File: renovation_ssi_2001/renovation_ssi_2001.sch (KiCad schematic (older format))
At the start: 70 parts, among them J1 KLPX-0848A-2-B, J2 DB15_Female, J4 Bus_ISA_8bit, J5 Pins_02x04, J6 Pins_02x03, J7 SID_Socket, Q1 PN2222A, Q2 PN2222A, U1 74LS74, U10 74LS138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

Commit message: corrections and improvements
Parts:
- added C21: 100nF, Capacitor_SMD:C_0603_1608Metric, symbol Device:C
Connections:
- net +12V: now also C21.1
- net GND: now also C21.2
- net LOWPASS: now also U12.40 (PB4); no longer U12.39 (PB3)
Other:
- moved on the sheet: C17, C18, C19, JP2, R10, R9, U11
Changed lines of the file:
@@
 Sheet 1 1
 Title "RENOVATION SSI-2001"
-Date "2020-02-16"
+Date "2020-03-08"
 Rev ""
 Comp "Benedikt Freisen"
@@
 Wire Wire Line
 	12000 4500 12400 4500
-Text Label 12650 7500 2    50   ~ 0
+Text Label 12650 7600 2    50   ~ 0
 LOWPASS
 Text Label 12400 4800 3    50   ~ 0
@@
 NoConn ~ 12650 7300
 NoConn ~ 12650 7400
-NoConn ~ 12650 7600
+NoConn ~ 12650 7500
 NoConn ~ 12650 7800
 NoConn ~ 12650 7900
@@
 L Device:R R9
 U 1 1 5E182A07
-P 12000 2550
-F 0 "R9" H 12070 2596 50  0000 L CNN
-F 1 "10k" H 12070 2505 50  0000 L CNN
-F 2 "Resistor_SMD:R_0603_1608Metric" V 11930 2550 50  0001 C CNN
-F 3 "~" H 12000 2550 50  0001 C CNN
-	1    12000 2550
+P 12500 2550
+F 0 "R9" H 12570 2596 50  0000 L CNN
+F 1 "10k" H 12570 2505 50  0000 L CNN
+F 2 "Resistor_SMD:R_0603_1608Metric" V 12430 2550 50  0001 C CNN
+F 3 "~" H 12500 2550 50  0001 C CNN
+	1    12500 2550
 	1    0    0    -1
 $EndComp
@@
 L Device:R R10
 U 1 1 5E183562
-P 12000 2850
-F 0 "R10" H 12070 2896 50  0000 L CNN
-F 1 "1k" H 12070 2805 50  0000 L CNN
-F 2 "Resistor_SMD:R_0603_1608Metric" V 11930 2850 50  0001 C CNN
-F 3 "~" H 12000 2850 50  0001 C CNN
-	1    12000 2850
+P 12500 2850
+F 0 "R10" H 12570 2896 50  0000 L CNN
+F 1 "1k" H 12570 2805 50  0000 L CNN
+F 2 "Resistor_SMD:R_0603_1608Metric" V 12430 2850 50  0001 C CNN
+F 3 "~" H 12500 2850 50  0001 C CNN
+	1    12500 2850
 	1    0    0    -1
 $EndComp
@@
 L Jumper:SolderJumper_2_Open JP2
 U 1 1 5E43CCF4
-P 14800 2400
-F 0 "JP2" H 14800 2605 50  0000 C CNN
-F 1 "SolderJumper_2_Open" H 14800 2514 50  0000 C CNN
-F 2 "Jumper:SolderJumper-2_P1.3mm_Open_RoundedPad1.0x1.5mm" H 14800 2400 50  0001 C CNN
-F 3 "~" H 14800 2400 50  0001 C CNN
-	1    14800 2400
-	1    0    0    -1
-$EndComp
-Wire Wire Line
-	12000 2400 11800 2400
-Wire Wire Line
-	11500 2700 12000 2700
-Connection ~ 12000 2700
-Connection ~ 12000 2400
-Wire Wire Line
-	12500 2400 12000 2400
-Connection ~ 12000 3000
+P 15050 2400
+F 0 "JP2" H 15050 2605 50  0000 C CNN
+F 1 "SolderJumper_2_Open" H 15050 2514 50  0000 C CNN
+F 2 "Jumper:SolderJumper-2_P1.3mm_Open_RoundedPad1.0x1.5mm" H 15050 2400 50  0001 C CNN
+F 3 "~" H 15050 2400 50  0001 C CNN
+	1    15050 2400
+	1    0    0    -1
+$EndComp
+Wire Wire Line
+	12500 2400 12300 2400
+Wire Wire Line
+	12000 2700 12500 2700
+Connection ~ 12500 2700
+Connection ~ 12500 2400
+Wire Wire Line
+	13000 2400 12500 2400
 $Comp
 L Device:R_Network09 RN2
@@
 	11000 3000 10800 3000
 Wire Wire Line
-	11000 3000 12000 3000
-Connection ~ 11000 3000
-Wire Wire Line
-	12500 2850 12500 3000
-Wire Wire Line
-	12500 2550 12500 2400
+	11000 3000 11500 3000
+Wire Wire Line
+	13000 2850 13000 3000
+Wire Wire Line
+	13000 2550 13000 2400
+Wire Wire Line
+	14000 2550 14000 2400
+Wire Wire Line
+	14000 2400 13500 2400
+Connection ~ 13000 2400
 Wire Wire Line
 	13500 2550 13500 2400
+Connection ~ 13500 2400
 Wire Wire Line
 	13500 2400 13000 2400
-Connection ~ 12500 2400
-Wire Wire Line
-	13000 2550 13000 2400
-Connection ~ 13000 2400
-Wire Wire Line
-	13000 2400 12500 2400
-Wire Wire Line
-	13500 2850 13500 3000
+Wire Wire Line
+	14000 2850 14000 3000
+Wire Wire Line
+	14000 3000 13500 3000
+Connection ~ 13000 3000
+Wire Wire Line
+	13500 3000 13500 2850
+Connection ~ 13500 3000
 Wire Wire Line
 	13500 3000 13000 3000
-Connection ~ 12500 3000
-Wire Wire Line
-	13000 3000 13000 2850
-Connection ~ 13000 3000
-Wire Wire Line
-	13000 3000 12500 3000
-Wire Wire Line
-	12000 3000 12500 3000
-Wire Wire Line
-	11000 2400 11200 2400
+Wire Wire Line
+	12500 3000 13000 3000
 $Comp
 L Regulator_Linear:LM1117-ADJ U11
 U 1 1 5E125189
-P 11500 2400
-F 0 "U11" H 11500 2642 50  0000 C CNN
-F 1 "LM1117-ADJ" H 11500 2551 50  0000 C CNN
-F 2 "Package_TO_SOT_SMD:SOT-223-3_TabPin2" H 11500 2400 50  0001 C CNN
-F 3 "http://www.ti.com/lit/ds/symlink/lm1117.pdf" H 11500 2400 50  0001 C CNN
-	1    11500 2400
+P 12000 2400
+F 0 "U11" H 12000 2642 50  0000 C CNN
+F 1 "LM1117-ADJ" H 12000 2551 50  0000 C CNN
+F 2 "Package_TO_SOT_SMD:SOT-223-3_TabPin2" H 12000 2400 50  0001 C CNN
+F 3 "http://www.ti.com/lit/ds/symlink/lm1117.pdf" H 12000 2400 50  0001 C CNN
+	1    12000 2400
 	1    0    0    -1
 $EndComp
@@
 L power:+12V #PWR0101
 U 1 1 5EB51AB3
-P 14200 2400
-F 0 "#PWR0101" H 14200 2250 50  0001 C CNN
-F 1 "+12V" H 14215 2573 50  0000 C CNN
-F 2 "" H 14200 2400 50  0001 C CNN
-F 3 "" H 14200 2400 50  0001 C CNN
-	1    14200 2400
-	1    0    0    -1
-$EndComp
-Wire Wire Line
-	14200 2400 14650 2400
+P 14500 2400
+F 0 "#PWR0101" H 14500 2250 50  0001 C CNN
+F 1 "+12V" H 14515 2573 50  0000 C CNN
+F 2 "" H 14500 2400 50  0001 C CNN
+F 3 "" H 14500 2400 50  0001 C CNN
+	1    14500 2400
+	1    0    0    -1
+$EndComp
 Wire Notes Line
 	11800 9950 11800 9800
@@
 L power:VDD #PWR0102
 U 1 1 5ED49FCE
-P 13700 2400
-F 0 "#PWR0102" H 13700 2250 50  0001 C CNN
-F 1 "VDD" H 13717 2573 50  0000 C CNN
-F 2 "" H 13700 2400 50  0001 C CNN
-F 3 "" H 13700 2400 50  0001 C CNN
-	1    13700 2400
+P 14200 2400
+F 0 "#PWR0102" H 14200 2250 50  0001 C CNN
+F 1 "VDD" H 14217 2573 50  0000 C CNN
+F 2 "" H 14200 2400 50  0001 C CNN
+F 3 "" H 14200 2400 50  0001 C CNN
+	1    14200 2400
 	1    0    0    -1
 $EndComp
@@
 L power:VDD #PWR0103
 U 1 1 5ED5E974
-P 15400 2400
-F 0 "#PWR0103" H 15400 2250 50  0001 C CNN
-F 1 "VDD" H 15417 2573 50  0000 C CNN
-F 2 "" H 15400 2400 50  0001 C CNN
-F 3 "" H 15400 2400 50  0001 C CNN
-	1    15400 2400
-	1    0    0    -1
-$EndComp
-Wire Wire Line
-	14950 2400 15400 2400
-Wire Wire Line
-	13700 2400 13500 2400
-Connection ~ 13500 2400
+P 15600 2400
+F 0 "#PWR0103" H 15600 2250 50  0001 C CNN
+F 1 "VDD" H 15617 2573 50  0000 C CNN
+F 2 "" H 15600 2400 50  0001 C CNN
+F 3 "" H 15600 2400 50  0001 C CNN
+	1    15600 2400
+	1    0    0    -1
+$EndComp
+Wire Wire Line
+	15200 2400 15600 2400
+Wire Wire Line
+	14200 2400 14000 2400
+Connection ~ 14000 2400
 $Comp
 L power:VDD #PWR0104
@@
 L Device:CP C17
 U 1 1 5E4CE257
-P 12500 2700
-F 0 "C17" H 12618 2746 50  0000 L CNN
-F 1 "22µF" H 12618 2655 50  0000 L CNN
-F 2 "Capacitor_Tantalum_SMD:CP_EIA-3528-21_Kemet-B" H 12538 2550 50  0001 C CNN
-F 3 "~" H 12500 2700 50  0001 C CNN
-	1    12500 2700
+P 13000 2700
+F 0 "C17" H 13118 2746 50  0000 L CNN
+F 1 "22µF" H 13118 2655 50  0000 L CNN
+F 2 "Capacitor_Tantalum_SMD:CP_EIA-3528-21_Kemet-B" H 13038 2550 50  0001 C CNN
+F 3 "~" H 13000 2700 50  0001 C CNN
+	1    13000 2700
 	1    0    0    -1
 $EndComp
@@
 L Device:C C18
 U 1 1 5E60F0A6
-P 13000 2700
-F 0 "C18" H 13115 2746 50  0000 L CNN
-F 1 "100nF" H 13115 2655 50  0000 L CNN
-F 2 "Capacitor_SMD:C_0603_1608Metric" H 13038 2550 50  0001 C CNN
-F 3 "~" H 13000 2700 50  0001 C CNN
-	1    13000 2700
-	1    0    0    -1
-$EndComp
-$Comp
-L Device:C C19
-U 1 1 5E60DD45
 P 13500 2700
-F 0 "C19" H 13615 2746 50  0000 L CNN
+F 0 "C18" H 13615 2746 50  0000 L CNN
 F 1 "100nF" H 13615 2655 50  0000 L CNN
 F 2 "Capacitor_SMD:C_0603_1608Metric" H 13538 2550 50  0001 C CNN
 F 3 "~" H 13500 2700 50  0001 C CNN
 	1    13500 2700
+	1    0    0    -1
+$EndComp
+$Comp
+L Device:C C19
+U 1 1 5E60DD45
+P 14000 2700
+F 0 "C19" H 14115 2746 50  0000 L CNN
+F 1 "100nF" H 14115 2655 50  0000 L CNN
+F 2 "Capacitor_SMD:C_0603_1608Metric" H 14038 2550 50  0001 C CNN
+F 3 "~" H 14000 2700 50  0001 C CNN
+	1    14000 2700
 	1    0    0    -1
 $EndComp
@@
 Wire Wire Line
 	5200 9600 5200 9700
-Text Notes 14100 3300 0    50   ~ 0
+Text Notes 14500 3300 0    50   ~ 0
 Note:\n\nSTM32: R9=10k, R10=1k\n\nMOS 6581: JP2 bridged\nU11, R9, R10, C17-C19 unpopulated\n\nMOS 8580: R9=1k, R10=2k\nC18, C19 unpopulated
 Text Notes 9700 5700 0    50   ~ 0
@@
 Text Notes 7100 2950 0    50   ~ 0
 Note:\nSTM32 does not need this. Leave\nunpopulated, open JP3 and add\nwire bridges where indicated on the PCB.
+$Comp
+L Device:C C21
+U 1 1 5E6AC39B
+P 11500 2700
+F 0 "C21" H 11615 2746 50  0000 L CNN
+F 1 "100nF" H 11615 2655 50  0000 L CNN
+F 2 "Capacitor_SMD:C_0603_1608Metric" H 11538 2550 50  0001 C CNN
+F 3 "~" H 11500 2700 50  0001 C CNN
+	1    11500 2700
+	1    0    0    -1
+$EndComp
+Wire Wire Line
+	14500 2400 14900 2400
+Connection ~ 11000 3000
+Wire Wire Line
+	11000 2400 11500 2400
+Wire Wire Line
+	11500 2400 11500 2550
+Connection ~ 11500 2400
+Wire Wire Line
+	11500 2400 11700 2400
+Wire Wire Line
+	11500 2850 11500 3000
+Connection ~ 11500 3000
+Wire Wire Line
+	11500 3000 12500 3000
+Connection ~ 12500 3000
 $EndSCHEMATC

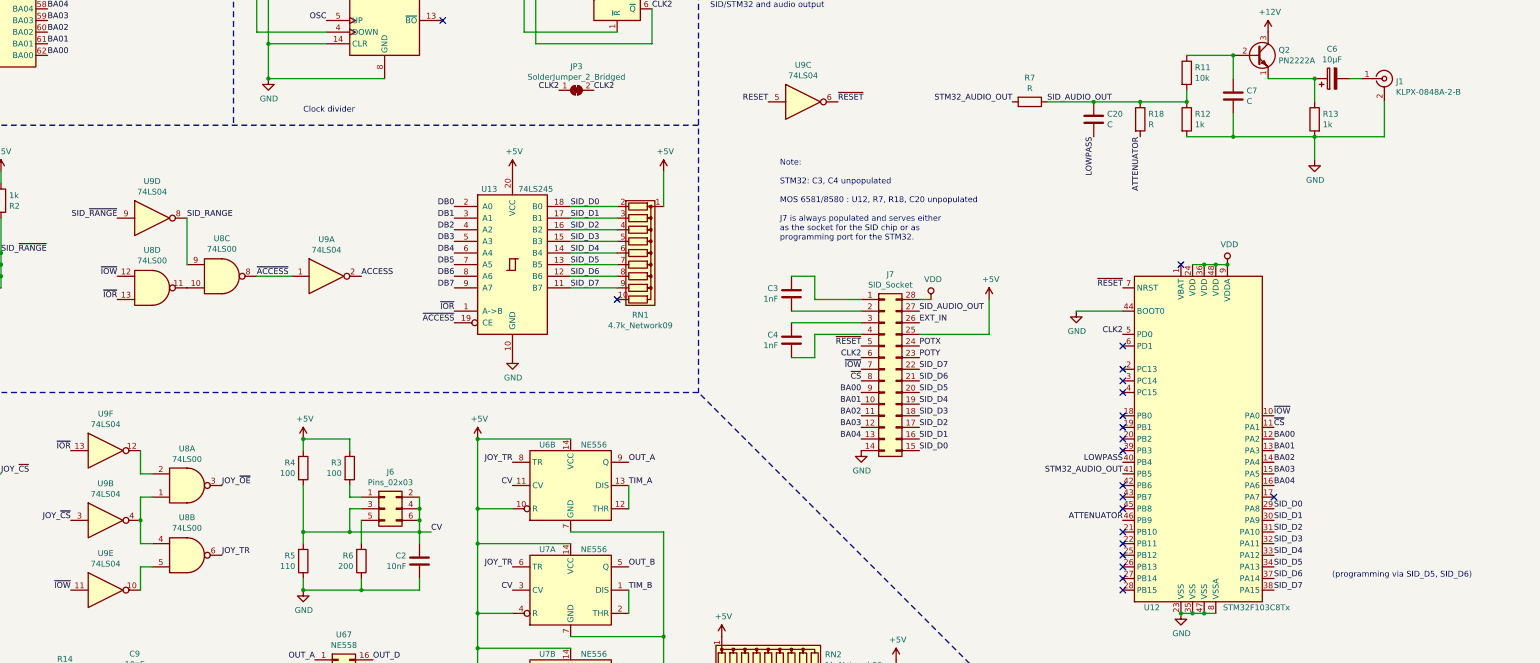
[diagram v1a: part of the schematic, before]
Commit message: fill in some component values, add pad to simplify fast ISA mod, adjust mounting hole positions
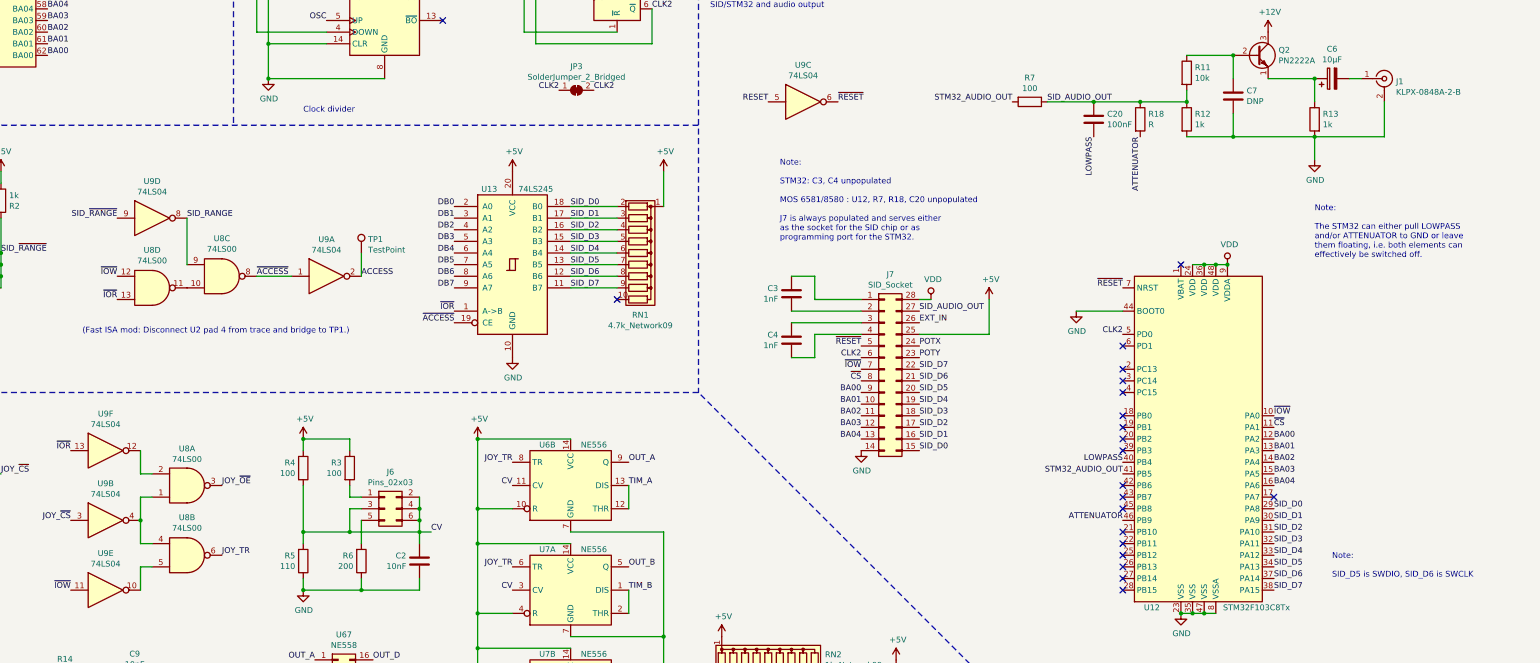
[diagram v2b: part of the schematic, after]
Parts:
- added TP1: TestPoint, TestPoint:TestPoint_Pad_1.5x1.5mm, symbol Connector:TestPoint
- C20: value C -> 100nF
- C7: value C -> DNP
- R7: value R -> 100
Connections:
- net ACCESS: now also TP1.1
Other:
- note added: "(Fast ISA mod: Disconnect U2 pad 4 from trace and bridge to TP1.)"
- note added: "Note:\n\nSID_D5 is SWDIO, SID_D6 is SWCLK"
- note added: "Note:\n\nThe STM32 can either pull LOWPASS\nand/or ATTENUATOR to GND or leave\nthem floating, i.e. both elements can\neffectively be switched off."
- note removed: "(programming via SID_D5, SID_D6)"
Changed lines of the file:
@@
 Sheet 1 1
 Title "RENOVATION SSI-2001"
-Date "2020-03-08"
+Date "2020-03-10"
 Rev ""
 Comp "Benedikt Freisen"
@@
 P 12400 4650
 F 0 "C20" H 12515 4696 50  0000 L CNN
-F 1 "C" H 12515 4605 50  0000 L CNN
+F 1 "100nF" H 12515 4605 50  0000 L CNN
 F 2 "Capacitor_SMD:C_0603_1608Metric" H 12438 4500 50  0001 C CNN
 F 3 "~" H 12400 4650 50  0001 C CNN
@@
 P 11850 4500
 F 0 "R7" V 11643 4500 50  0000 C CNN
-F 1 "R" V 11734 4500 50  0000 C CNN
+F 1 "100" V 11734 4500 50  0000 C CNN
 F 2 "Resistor_SMD:R_0603_1608Metric" V 11780 4500 50  0001 C CNN
 F 3 "~" H 11850 4500 50  0001 C CNN
@@
 NoConn ~ 13950 7900
 Text Notes 14450 8600 0    50   ~ 0
-(programming via SID_D5, SID_D6)
+Note:\n\nSID_D5 is SWDIO, SID_D6 is SWCLK
 NoConn ~ 12650 7200
 NoConn ~ 12650 7300
@@
 P 13600 4450
 F 0 "C7" H 13485 4404 50  0000 R CNN
-F 1 "C" H 13485 4495 50  0000 R CNN
+F 1 "DNP" H 13485 4495 50  0000 R CNN
 F 2 "SSI_2001:C_Disc_D3.4mm_W2.1mm_P2.50mm_alt" H 13638 4300 50  0001 C CNN
 F 3 "~" H 13600 4450 50  0001 C CNN
@@
 	11500 3000 12500 3000
 Connection ~ 12500 3000
+Text Notes 14300 5850 0    50   ~ 0
+Note:\n\nThe STM32 can either pull LOWPASS\nand/or ATTENUATOR to GND or leave\nthem floating, i.e. both elements can\neffectively be switched off.
+$Comp
+L Connector:TestPoint TP1
+U 1 1 5E69B41B
+P 6100 5800
+F 0 "TP1" H 6158 5918 50  0000 L CNN
+F 1 "TestPoint" H 6158 5827 50  0000 L CNN
+F 2 "TestPoint:TestPoint_Pad_1.5x1.5mm" H 6300 5800 50  0001 C CNN
+F 3 "~" H 6300 5800 50  0001 C CNN
+	1    6100 5800
+	1    0    0    -1
+$EndComp
+Wire Wire Line
+	6100 5800 6100 6000
+Text Notes 3700 6500 0    50   ~ 0
+(Fast ISA mod: Disconnect U2 pad 4 from trace and bridge to TP1.)
 $EndSCHEMATC
